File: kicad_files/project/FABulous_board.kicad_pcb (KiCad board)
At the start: 2 copper layers, 61 parts, among them J2 Conn_01x02_Socket, SW1 Tactile Switch, T1 Logo, U1 W25Q32FVSS, U10 SN74LVC1G125DCKR, U2 caravel-M.2-card, U3 Caravel_WCSP, U4 U241-041N-1WR85-1_C2880605, U5 FT232H, U6 AMS1117-3_3, U7 SPX1117M3-L-1-5_TR, U8 MCP1319MT-29LE-OT, U9 SN74LVC1G125DCKR, X1 TXM12M0004252DBCEO00T

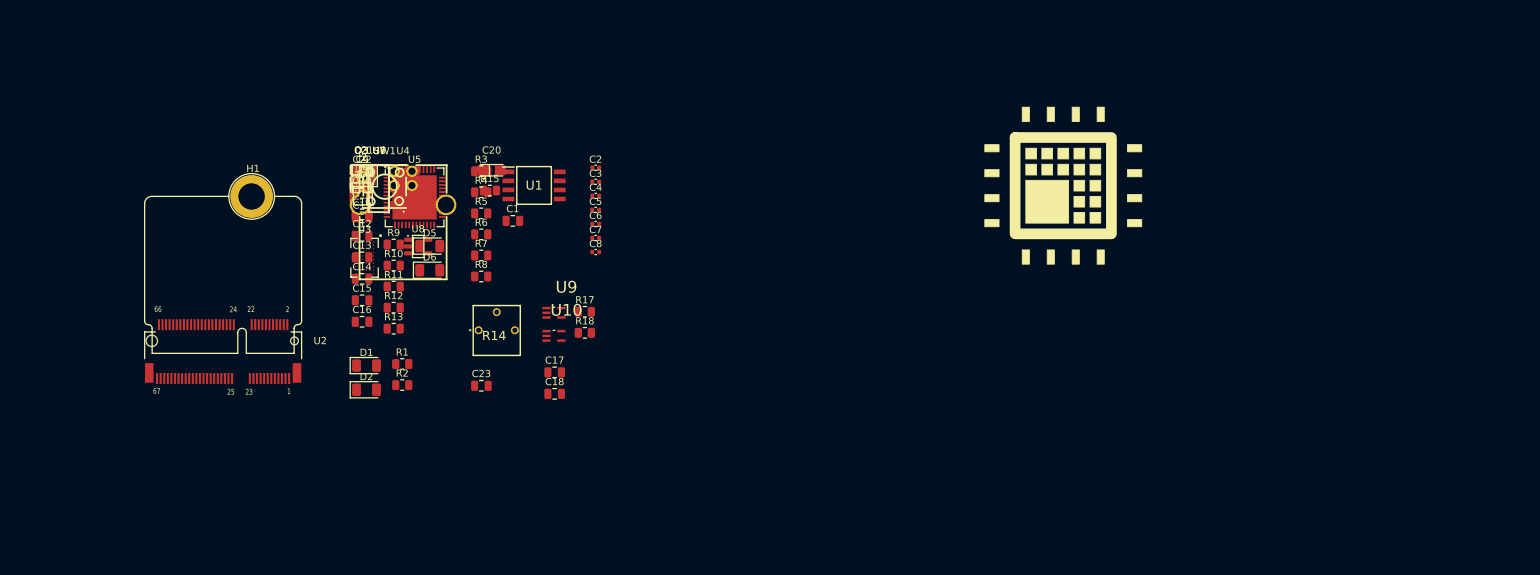
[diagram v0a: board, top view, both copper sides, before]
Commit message: started with board layout, also added more stuff on the schematic
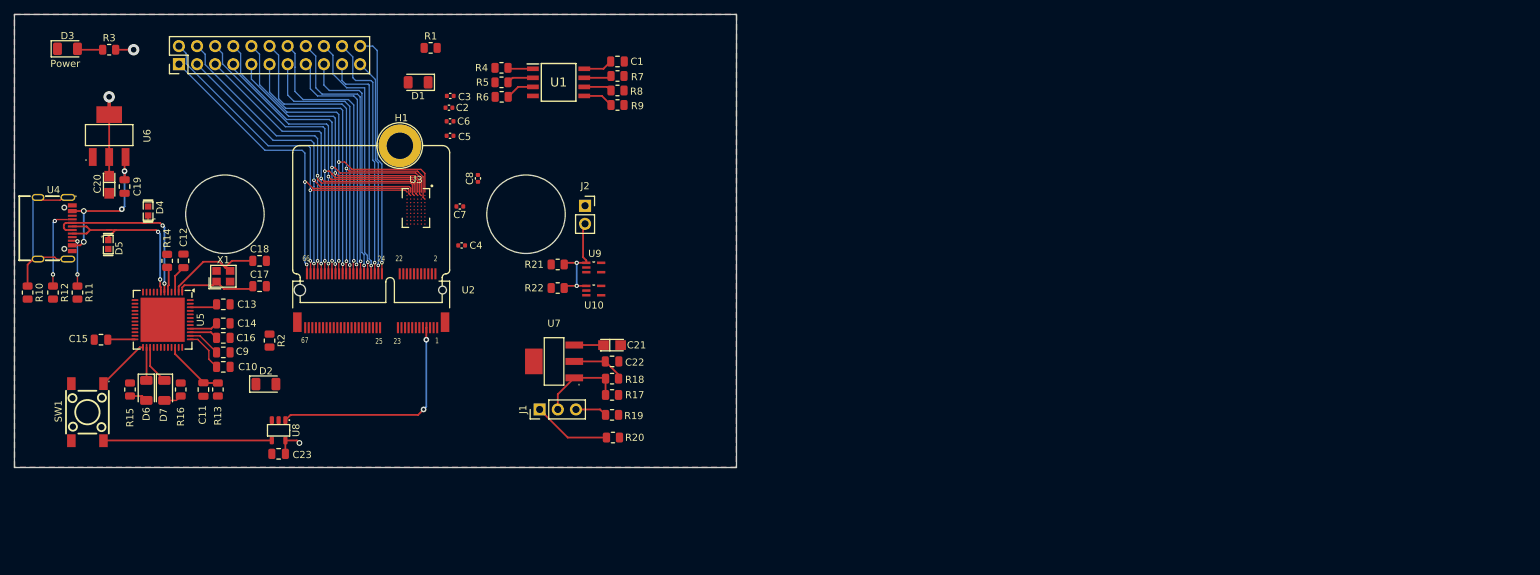
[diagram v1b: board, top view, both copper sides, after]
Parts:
- removed the R14 at (87.6, 102.8)
- removed the R15 at (86.6, 79.7)
- removed the R9 at (73.2, 87.2)
- removed T1: Logo, FABulous:logo
- added D2: red, LED_SMD:LED_1206_3216Metric, F.Cu at (55.2, 106.8)
- added J1: Conn_01x03_Pin, Connector_PinHeader_2.54mm:PinHeader_1x03_P2.54mm_Vertical, F.Cu at (93.6, 110.4)
- added J3: Conn_02x11_Odd_Even, Connector_PinHeader_2.54mm:PinHeader_2x11_P2.54mm_Vertical, F.Cu at (43.1, 62.0)
- added R10: 0, Resistor_SMD:R_0805_2012Metric, F.Cu at (21.8, 94.0)
- added R11: 5.1k, Resistor_SMD:R_0805_2012Metric, F.Cu at (28.8, 94.0)
- added R12: 5.1k, Resistor_SMD:R_0805_2012Metric, F.Cu at (25.4, 94.0)
- added R17: 220, Resistor_SMD:R_0805_2012Metric, F.Cu at (103.8, 108.3)
- added R18: 510, Resistor_SMD:R_0805_2012Metric, F.Cu at (103.8, 106.0)
- added R19: 330, Resistor_SMD:R_0805_2012Metric, F.Cu at (103.8, 111.1)
- added R2: 82, Resistor_SMD:R_0805_2012Metric, F.Cu at (55.8, 100.7)
- added R20: 120, Resistor_SMD:R_0805_2012Metric, F.Cu at (103.9, 114.3)
- C17: value 0pF -> 10pF
- U2: value caravel-M.2-card -> ~
- U3: value Caravel_WCSP -> ~
- U4: value U241-041N-1WR85-1_C2880605 -> GT-USB-7010ASV; footprint easy_eda:USB-B-TH_AMPHENOL_61729-0010BLF -> easy_eda:USB-C-SMD_G-SWITCH_GT-USB-7010ASV
- moved D3 61.1 mm to (27.4, 59.8)
- moved R3 60.2 mm to (33.3, 59.9), turned to 180 degrees
- moved C20 53.6 mm to (33.3, 78.9), turned to -90 degrees
- moved SW1 52.3 mm to (30.2, 110.7), turned to -90 degrees
- moved U4 49.1 mm to (25.7, 85.0), turned to -90 degrees
- moved R1 47.4 mm to (78.3, 59.7)
- moved C18 45.4 mm to (54.4, 89.5), turned to 180 degrees
- moved D6 44.6 mm to (38.5, 107.7), turned to -90 degrees
- moved C22 44.0 mm to (103.8, 103.6)
- moved D1 43.7 mm to (76.6, 64.5), turned to 180 degrees
- moved C17 43.1 mm to (54.4, 93.1), turned to 180 degrees
- moved C21 42.6 mm to (103.8, 101.3)
- moved D7 40.8 mm to (41.0, 107.7), turned to -90 degrees
- moved U5 39.3 mm to (40.8, 97.8), turned to -90 degrees
- moved R15 38.7 mm to (36.2, 107.6), turned to 90 degrees
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- renumbered C11 to C10, C9 to C11, C10 to C9, D2 to D1, D1 to D3, D3 to D4, D4 to D5, D5 to D6, D6 to D7, R2 to R1, R10 to R13, R11 to R14, R12 to R15, R13 to R16, R17 to R21, R18 to R22, R1 to R3, R3 to R4, R4 to R5, R5 to R6, R6 to R7, R7 to R8, R8 to R9
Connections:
- net /Caravel Connections/mprj_io.7 renamed /Caravel Connections/FC.external_clock
- net /Caravel Connections/mprj_io.8 renamed /Caravel Connections/FC.clock_select_0
- net /Caravel Connections/mprj_io.9 renamed /Caravel Connections/FC.clock_select_1
- net Net-(D5-K) renamed /PC connection/RX_LED
- net Net-(D6-K) renamed /PC connection/TX_LED
- net Net-(U5-REF) renamed /PC connection/REF
- net Net-(U5-VCCA) renamed /PC connection/VCCA
- net Net-(U5-VCCCORE) renamed /PC connection/VCCCORE
- net Net-(U5-~{RESET}) renamed /PC connection/~{RESET}
- D4 pad 1: Net-(U4-D-) -> /PC connection/D-
- D5 pad 1: Net-(U4-D+) -> /PC connection/D+
- U2 pad 49: /Caravel Connections/mprj_io.0 -> unconnected-(U2-mprj_io[0]-Pad49)
- U2 pad 73: /Caravel Connections/mprj_io.12 -> /Caravel Connections/fpga_rx_led
- U2 pad 75: /Caravel Connections/mprj_io.13 -> /Caravel Connections/fpga_uart_rx
- U3 pad C9: /Caravel Connections/xlck -> /Caravel Connections/xclk
- U3 pad D3: /Caravel Connections/mprj_io.13 -> /Caravel Connections/fpga_rx_led
- U3 pad D7: /Caravel Connections/mprj_io.0 -> unconnected-(U3-mprj_io[0]_JTAG-PadD7)
- U3 pad F3: /Caravel Connections/mprj_io.12 -> /Caravel Connections/fpga_uart_rx
- U4 pad 1: +5V -> /PC connection/Shield
- U4 pad 2: Net-(U4-D-) -> /PC connection/Shield
- U4 pad 3: Net-(U4-D+) -> /PC connection/Shield
- U4 pad 4: GND -> /PC connection/Shield
- U5 pad 6: Net-(U4-D-) -> /PC connection/D-
- U5 pad 7: Net-(U4-D+) -> /PC connection/D+
- U7 pad 1: Net-(R14-CCW) -> /Power conversion/ADJ
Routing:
- net /Caravel Connections/mprj_io.17: track 0.00 -> 57.8 mm, vias 0 -> 2
- net /Caravel Connections/mprj_io.19: track 0.00 -> 56.6 mm, vias 0 -> 2
- net /Caravel Connections/mprj_io.15: track 0.00 -> 56.5 mm, vias 0 -> 2
- net /Caravel Connections/mprj_io.23: track 0.00 -> 56.4 mm, vias 0 -> 2
- net /Caravel Connections/mprj_io.21: track 0.00 -> 56.2 mm, vias 0 -> 2
- net /Caravel Connections/mprj_io.14: track 0.00 -> 55.8 mm, vias 0 -> 2
- net /Caravel Connections/mprj_io.25: track 0.00 -> 55.6 mm, vias 0 -> 2
- net /Caravel Connections/mprj_io.16: track 0.00 -> 54.5 mm, vias 0 -> 2
- net /Caravel Connections/mprj_io.18: track 0.00 -> 53.1 mm, vias 0 -> 2
- net /Caravel Connections/mprj_io.20: track 0.00 -> 52.5 mm, vias 0 -> 2
- net /Caravel Connections/mprj_io.22: track 0.00 -> 52.4 mm, vias 0 -> 2
- net +3V3: track 0.00 -> 41.4 mm, vias 0 -> 3
- net /Caravel Connections/mprj_io.27: track 0.00 -> 39.5 mm, vias 0 -> 1
- net /Caravel Connections/mprj_io.24: track 0.00 -> 38.1 mm, vias 0 -> 1
- net /Caravel Connections/mprj_io.29: track 0.00 -> 38.0 mm, vias 0 -> 1
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- added copper zone on In2.Cu, net +3V3
- added copper zone on B.Cu, net GND
- added copper zone on F.Cu, net GND
- added copper zone on In1.Cu, net GND
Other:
- board outline added: 101.2 x 63.5 mm
- copper layers 2 -> 4
- board text added: "Power"

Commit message: new layout, add more pin header, change the caravel power pin supply
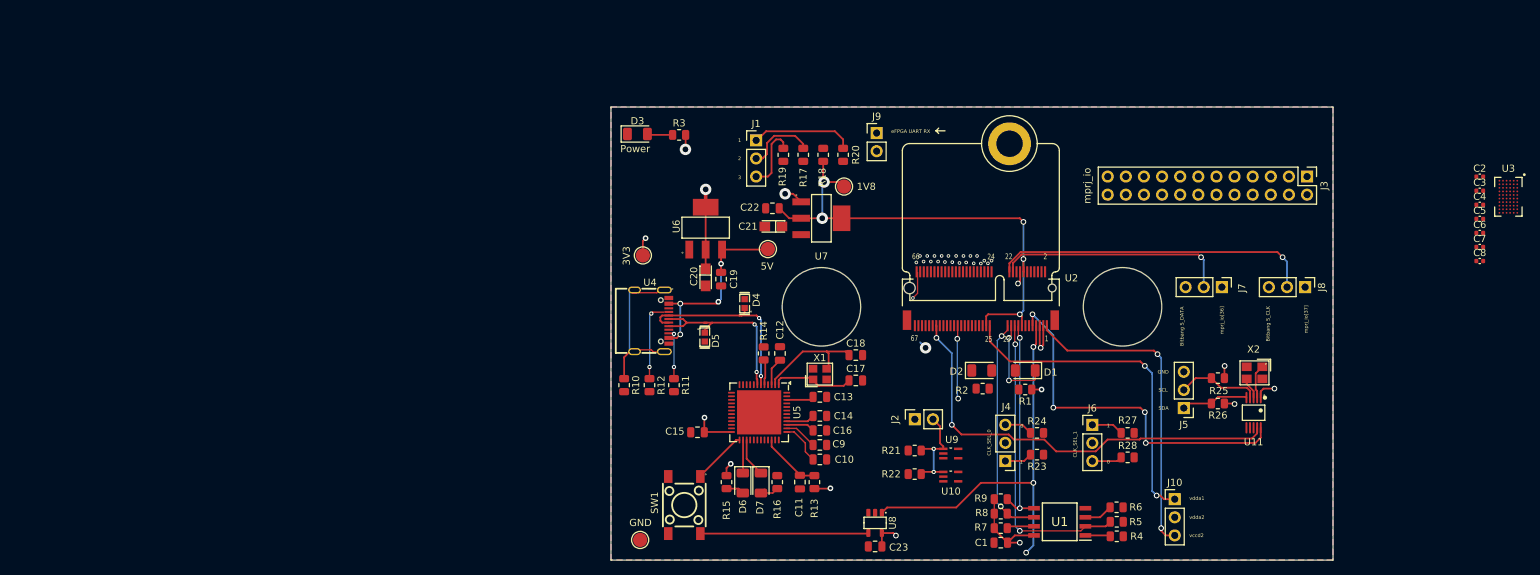
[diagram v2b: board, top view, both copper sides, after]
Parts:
- added J10: Conn_01x03_Pin, Connector_PinHeader_2.54mm:PinHeader_1x03_P2.54mm_Vertical, F.Cu at (182.6, 122.9)
- added J4: Conn_01x03_Pin, Connector_PinHeader_2.54mm:PinHeader_1x03_P2.54mm_Vertical, F.Cu at (158.9, 117.6)
- added J5: Conn_01x03_Pin, Connector_PinHeader_2.54mm:PinHeader_1x03_P2.54mm_Vertical, F.Cu at (183.9, 110.2)
- added J6: Conn_01x03_Pin, Connector_PinHeader_2.54mm:PinHeader_1x03_P2.54mm_Vertical, F.Cu at (171.1, 112.5)
- added J7: Conn_01x03_Pin, Connector_PinHeader_2.54mm:PinHeader_1x03_P2.54mm_Vertical, F.Cu at (189.2, 93.2)
- added J8: Conn_01x03_Pin, Connector_PinHeader_2.54mm:PinHeader_1x03_P2.54mm_Vertical, F.Cu at (200.9, 93.2)
- added J9: Conn_01x02_Pin, Connector_PinHeader_2.54mm:PinHeader_1x02_P2.54mm_Vertical, F.Cu at (140.8, 71.6)
- added R23: R, Resistor_SMD:R_0805_2012Metric, F.Cu at (163.3, 116.7)
- added R24: R, Resistor_SMD:R_0805_2012Metric, F.Cu at (163.3, 113.7)
- added R25: 2k, Resistor_SMD:R_0805_2012Metric, F.Cu at (188.7, 106.0)
- added R26: 2k, Resistor_SMD:R_0805_2012Metric, F.Cu at (188.7, 109.5)
- added R27: R, Resistor_SMD:R_0805_2012Metric, F.Cu at (176.0, 113.7)
- added R28: R, Resistor_SMD:R_0805_2012Metric, F.Cu at (176.0, 117.1)
- added TP1: TestPoint, TestPoint:TestPoint_Pad_D2.0mm, F.Cu at (107.7, 128.7)
- added TP2: TestPoint, TestPoint:TestPoint_Pad_D2.0mm, F.Cu at (108.1, 88.8)
- added TP3: TestPoint, TestPoint:TestPoint_Pad_D2.0mm, F.Cu at (125.6, 87.9)
- added TP4: TestPoint, TestPoint:TestPoint_Pad_D2.0mm, F.Cu at (136.3, 79.1)
- added U11: SI5351A-B-GTR, easy_eda:MSOP-10_L3.0-W3.0-P0.50-LS5.0-BL, F.Cu at (193.7, 110.8)
- added X2: NX3225GA-25_000M-STD-CRG-2, easy_eda:CRYSTAL-SMD_4P-L3.2-W2.5-BL, F.Cu at (193.8, 105.2)
- J3: value Conn_02x11_Odd_Even -> Conn_02x12_Odd_Even; footprint Connector_PinHeader_2.54mm:PinHeader_2x11_P2.54mm_Vertical -> Connector_PinHeader_2.54mm:PinHeader_2x12_P2.54mm_Vertical
- U3: footprint Caravel_Board:Caravel_WCSP -> Caravel_Board:Caravel_WCSP_0_25_mm_bga
- moved J3 158.9 mm to (201.2, 77.7), turned to -90 degrees
- moved U3 153.1 mm to (229.4, 80.6)
- moved C6 145.2 mm to (225.4, 85.6)
- moved C3 144.9 mm to (225.4, 79.7)
- moved C2 144.8 mm to (225.4, 77.7), turned to 0 degrees
- moved C5 144.8 mm to (225.4, 83.7)
- moved C7 143.1 mm to (225.4, 87.6), turned to 0 degrees
- moved C4 142.8 mm to (225.4, 81.7)
- moved C8 140.9 mm to (225.4, 89.6), turned to 0 degrees
- moved R4 108.4 mm to (174.5, 128.1), turned to 180 degrees
- moved R5 106.0 mm to (174.5, 126.1), turned to 180 degrees
- moved R6 103.6 mm to (174.5, 124.1), turned to 180 degrees
- moved D2 100.3 mm to (155.6, 104.9)
- moved R2 100.2 mm to (155.7, 107.4), turned to 0 degrees
- moved R1 96.1 mm to (161.7, 107.6), turned to 180 degrees
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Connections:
- net /Caravel Connections/FC.clock_select_0 renamed /FC.clock_select_0
- net /Caravel Connections/FC.clock_select_1 renamed /FC.clock_select_1
- net /Caravel Connections/FC.external_clock renamed /FC.external_clock
- net /Caravel Connections/fpga_uart_rx renamed /efpga_uart_rx
- net /Caravel Connections/xclk renamed /CLK_caravel
- net /Flash/~{MEM_HOLD} renamed Net-(U1-~{HOLD}(D3))
- net /Flash/~{MEM_WP} renamed Net-(U1-~{WP}(D2))
- SW1 pad 2: /PC connection/~{MR} -> GND
- SW1 pad 3: GND -> /PC connection/~{MR}
- U2 pad 15: /Caravel Connections/vcdd -> +1V8
- U2 pad 20: /Caravel Connections/Bitbang.S_DATA -> /Caravel Connections/mprj_io_37_internal
- U2 pad 22: /Caravel Connections/Bitbang.S_CLK -> /Caravel Connections/mprj_io_36_internal
- U3 pad A9: /Caravel Connections/Bitbang.S_DATA -> /Caravel Connections/mprj_io_37_internal
- U3 pad B9: /Caravel Connections/Bitbang.S_CLK -> /Caravel Connections/mprj_io_36_internal
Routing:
- net +1V8: track 7.53 -> 69.0 mm, vias 0 -> 5
- net /FC.external_clock: track 0.00 -> 61.0 mm, vias 0 -> 2
- net /Caravel Connections/mprj_io.17: track 57.8 -> 0.00 mm, vias 2 -> 1
- net /Caravel Connections/mprj_io.19: track 56.6 -> 0.00 mm, vias 2 -> 1
- net /Caravel Connections/mprj_io.23: track 56.4 -> 0.00 mm, vias 2 -> 1
- net /Caravel Connections/mprj_io.21: track 56.2 -> 0.00 mm, vias 2 -> 1
- net /Caravel Connections/mprj_io.25: track 55.6 -> 0.00 mm, vias 2 -> 1
- net /Caravel Connections/mprj_io.15: track 56.5 -> 1.37 mm
- net /Caravel Connections/mprj_io.16: track 54.5 -> 0.00 mm, vias 2 -> 1
- net /Caravel Connections/mprj_io.18: track 53.1 -> 0.00 mm, vias 2 -> 1
- net /Caravel Connections/mprj_io.20: track 52.5 -> 0.00 mm, vias 2 -> 1
- net /Caravel Connections/mprj_io.22: track 52.4 -> 0.00 mm, vias 2 -> 1
- net /Caravel Connections/mprj_io.14: track 55.8 -> 4.00 mm
- net /CLK_caravel: track 0.00 -> 51.2 mm, vias 0 -> 4
- net /Caravel Connections/vdda1: track 0.00 -> 47.0 mm, vias 0 -> 2
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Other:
- board text added: "0"
- board text added: "1"
- board text added: "1V8"
- board text added: "2"
- board text added: "3"
- board text added: "3V3"
- board text added: "5V"
- board text added: "Bitbang S_CLK"
- board text added: "Bitbang S_DATA"
- board text added: "CLK_SEL_0"
- board text added: "CLK_SEL_1"
- board text added: "GND"
- board text added: "SCL"
- board text added: "SDA"
- board text added: "eFPGA UART RX"
- board text added: "mprj_io"
- board text added: "mprj_io[36]"
- board text added: "mprj_io[37]"
- board text added: "vccd2"
- board text added: "vdda1"
- board text added: "vdda2"

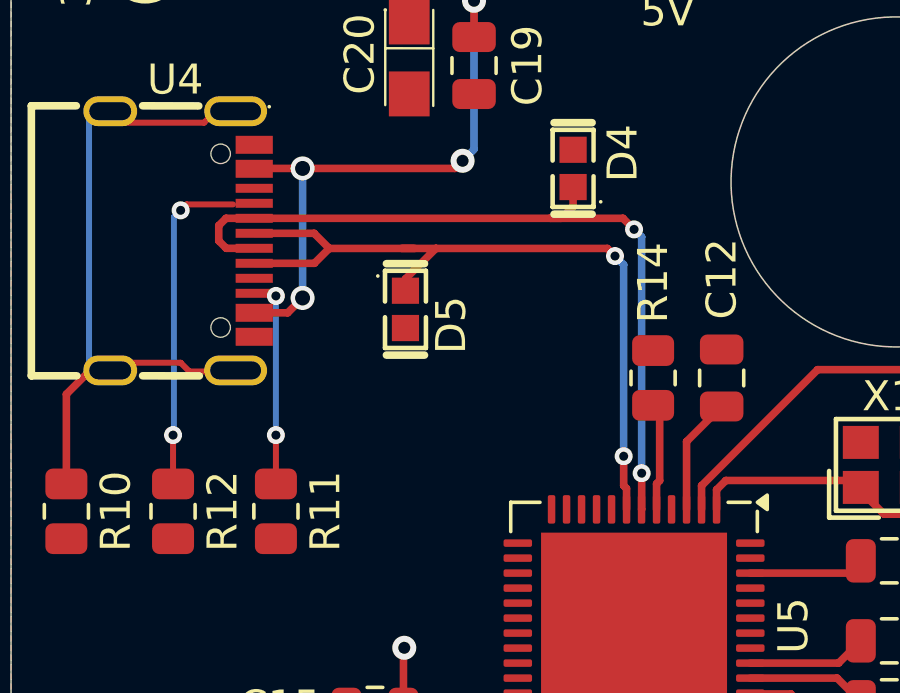
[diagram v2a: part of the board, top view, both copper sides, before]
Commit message: misc: simplifiy power pins and other components, add test pins
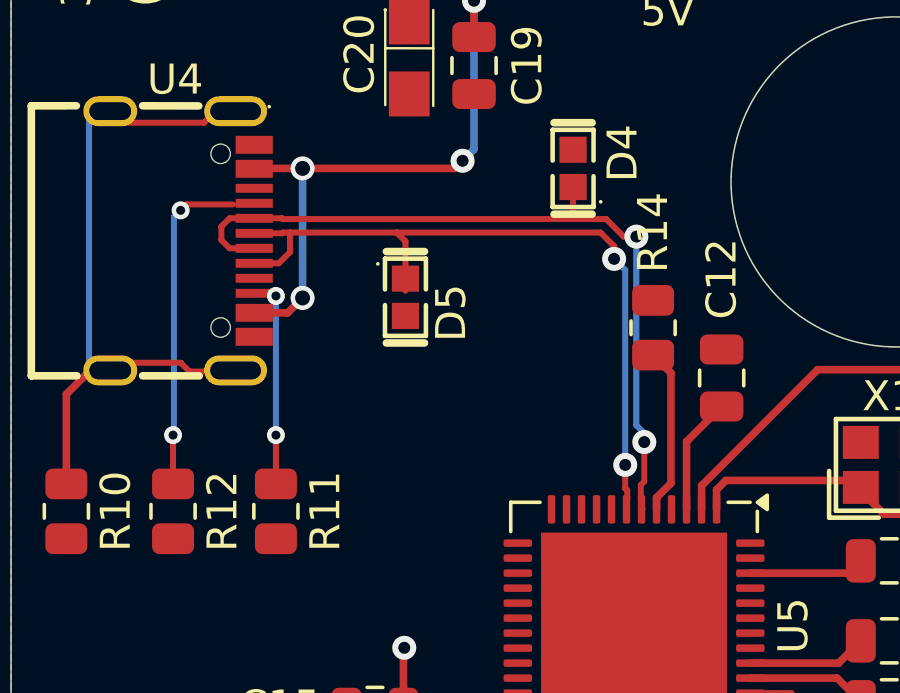
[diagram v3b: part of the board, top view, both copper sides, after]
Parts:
- moved R14 1.67 mm to (125.0, 100.8)
- moved D5 0.40 mm to (116.8, 99.8)
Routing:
- net /PC connection/REF: track 3.60 -> 5.59 mm
- net /PC connection/D+: track 25.9 -> 25.2 mm
- net /PC connection/D-: track 26.9 -> 26.3 mm
